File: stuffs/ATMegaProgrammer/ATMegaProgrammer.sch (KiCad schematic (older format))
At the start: 4 parts, among them CON1 AVR-ISP-6, IC1 ATMEGA328P-P, P1 CONN_01X14, P2 CONN_01X14

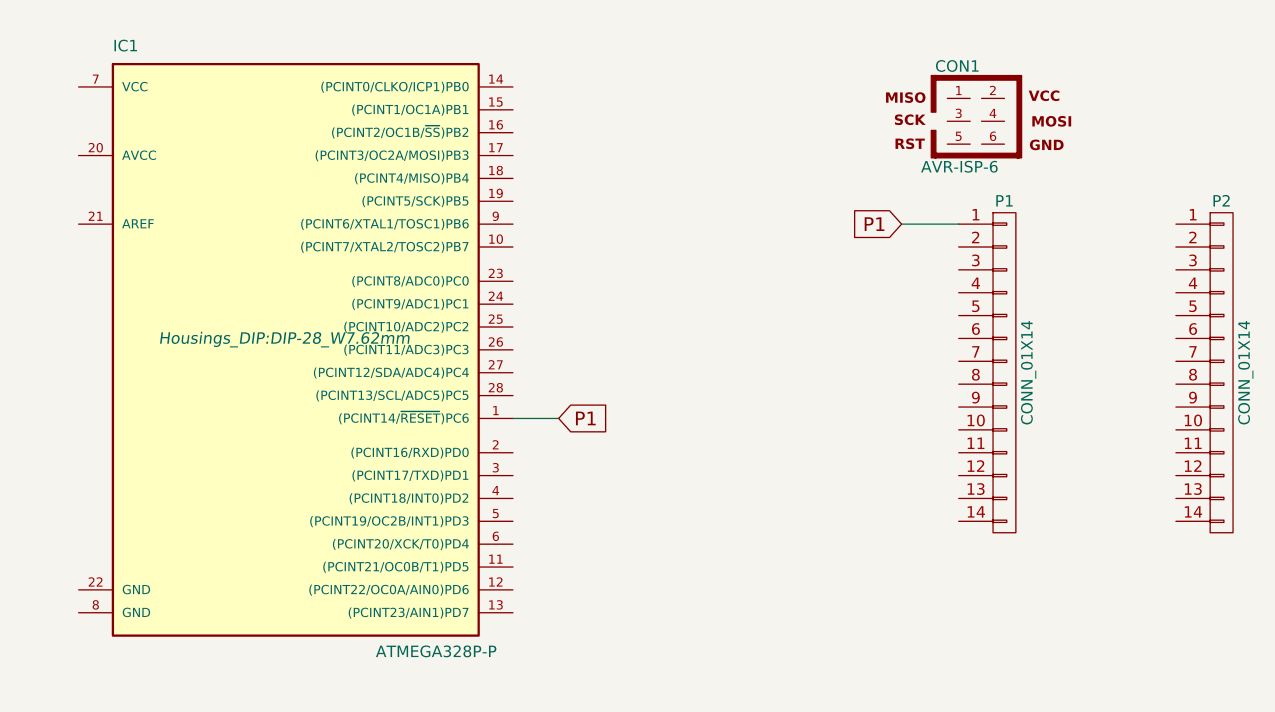
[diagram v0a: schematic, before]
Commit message: Improve ATMega328Programmer.
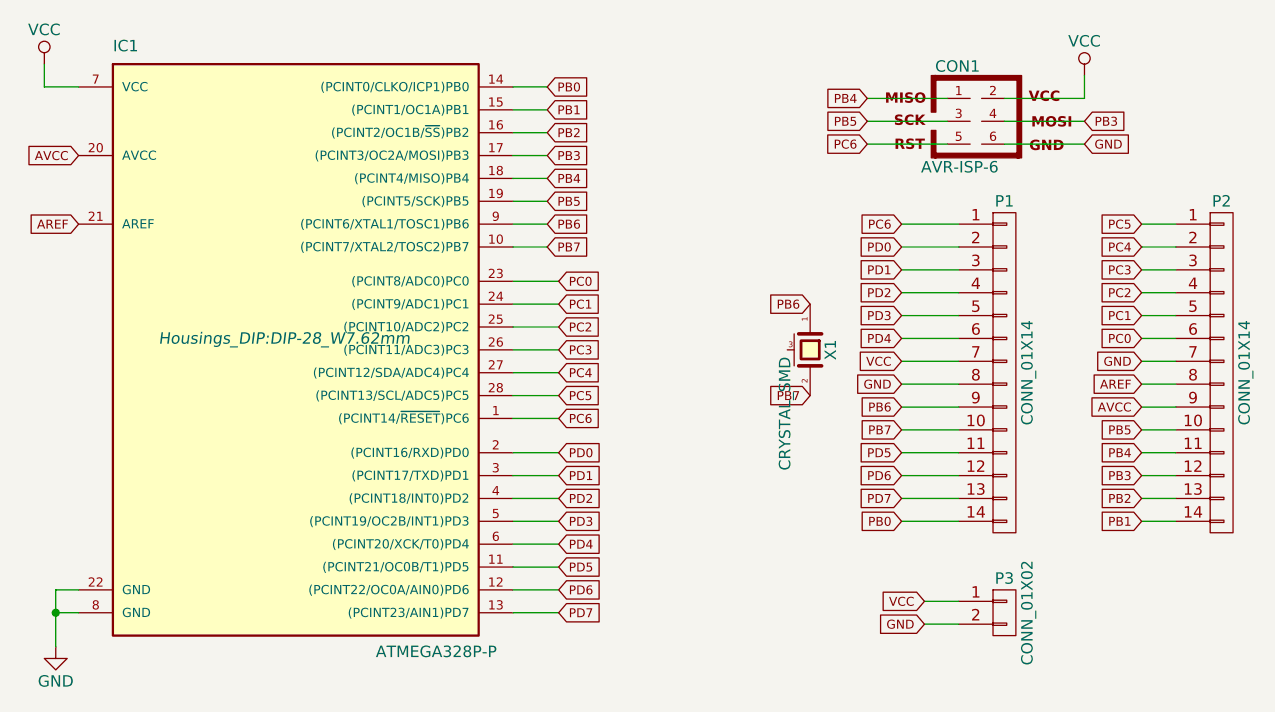
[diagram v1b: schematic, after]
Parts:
- added P3: CONN_01X02, Pin_Headers:Pin_Header_Straight_1x02, symbol CONN_01X02
- added X1: CRYSTAL_SMD, Crystals:crystal_FA238-TSX3225, symbol CRYSTAL_SMD
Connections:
- net P1 is gone; now on net PC6: IC1.1 ((PCINT14/~RESET~)PC6), P1.1 (P1)
- net PB7: now reaches IC1.10 ((PCINT7/XTAL2/TOSC2)PB7)
- net PB7: now also P1.10 (P10), X1.2
- net PD5: now reaches IC1.11 ((PCINT21/OC0B/T1)PD5)
- net PD5: now also P1.11 (P11)
- net PD6: now reaches IC1.12 ((PCINT22/OC0A/AIN0)PD6)
- net PD6: now also P1.12 (P12)
- net PD7: now reaches IC1.13 ((PCINT23/AIN1)PD7)
- net PD7: now also P1.13 (P13)
- net PB0: now reaches IC1.14 ((PCINT0/CLKO/ICP1)PB0)
- net PB0: now also P1.14 (P14)
- net PB1: now reaches IC1.15 ((PCINT1/OC1A)PB1)
- net PB1: now also P2.14 (P14)
- net PB2: now reaches IC1.16 ((PCINT2/OC1B/~SS~)PB2)
- net PB2: now also P2.13 (P13)
- net PB3: now reaches IC1.17 ((PCINT3/OC2A/MOSI)PB3)
- net PB3: now also CON1.4, P2.12 (P12)
- net PB4: now reaches IC1.18 ((PCINT4/MISO)PB4)
- net PB4: now also CON1.1, P2.11 (P11)
- net PB5: now reaches IC1.19 ((PCINT5/SCK)PB5)
- net PB5: now also CON1.3, P2.10 (P10)
- net PD0: now reaches IC1.2 ((PCINT16/RXD)PD0)
- net PD0: now also P1.2 (P2)
- net AVCC: now reaches IC1.20 (AVCC)
- net AVCC: now also P2.9 (P9)
- net AREF: now reaches IC1.21 (AREF)
- net AREF: now also P2.8 (P8)
- net GND: now reaches IC1.22 (GND)
- net GND: now also CON1.6, IC1.8 (GND), P1.8 (P8), P2.7 (P7), P3.2 (P2)
- net PC0: now reaches IC1.23 ((PCINT8/ADC0)PC0)
- net PC0: now also P2.6 (P6)
- net PC1: now reaches IC1.24 ((PCINT9/ADC1)PC1)
- net PC1: now also P2.5 (P5)
- net PC2: now reaches IC1.25 ((PCINT10/ADC2)PC2)
- net PC2: now also P2.4 (P4)
- net PC3: now reaches IC1.26 ((PCINT11/ADC3)PC3)
- net PC3: now also P2.3 (P3)
- net PC4: now reaches IC1.27 ((PCINT12/SDA/ADC4)PC4)
- net PC4: now also P2.2 (P2)
- net PC5: now reaches IC1.28 ((PCINT13/SCL/ADC5)PC5)
- net PC5: now also P2.1 (P1)
- net PD1: now reaches IC1.3 ((PCINT17/TXD)PD1)
- net PD1: now also P1.3 (P3)
- net PD2: now reaches IC1.4 ((PCINT18/INT0)PD2)
- net PD2: now also P1.4 (P4)
- net PD3: now reaches IC1.5 ((PCINT19/OC2B/INT1)PD3)
- net PD3: now also P1.5 (P5)
- net PD4: now reaches IC1.6 ((PCINT20/XCK/T0)PD4)
- net PD4: now also P1.6 (P6)
- net VCC: now reaches IC1.7 (VCC)
- net VCC: now also CON1.2, P1.7 (P7), P3.1 (P1)
- net PB6: now reaches IC1.9 ((PCINT6/XTAL1/TOSC1)PB6)
- net PB6: now also P1.9 (P9), X1.1
- net PC6: now reaches CON1.5

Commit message: Add ground planes, fix labels and connect GND for crystal.
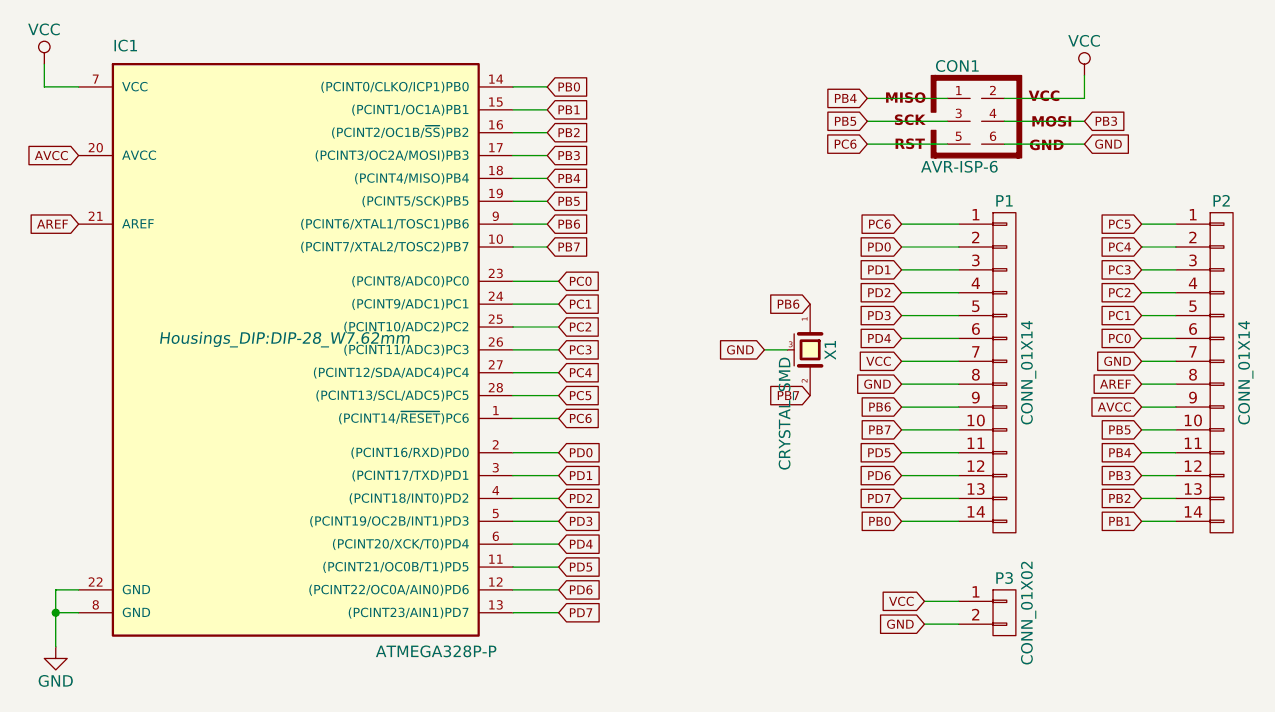
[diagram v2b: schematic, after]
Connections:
- net GND: now also X1.3 (case)
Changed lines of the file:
@@
 Text GLabel 4700 2850 0    39   Input ~ 0
 PB6
+Wire Wire Line
+	4600 3050 4500 3050
+Text GLabel 4500 3050 0    39   Input ~ 0
+GND
 $EndSCHEMATC
